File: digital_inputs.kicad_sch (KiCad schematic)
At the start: 12 parts, among them J3 Samtec Isorate, J5 Samtec Isorate, U6 SN74LV8T9541-EP, U7 SN74LV8T9541-EP

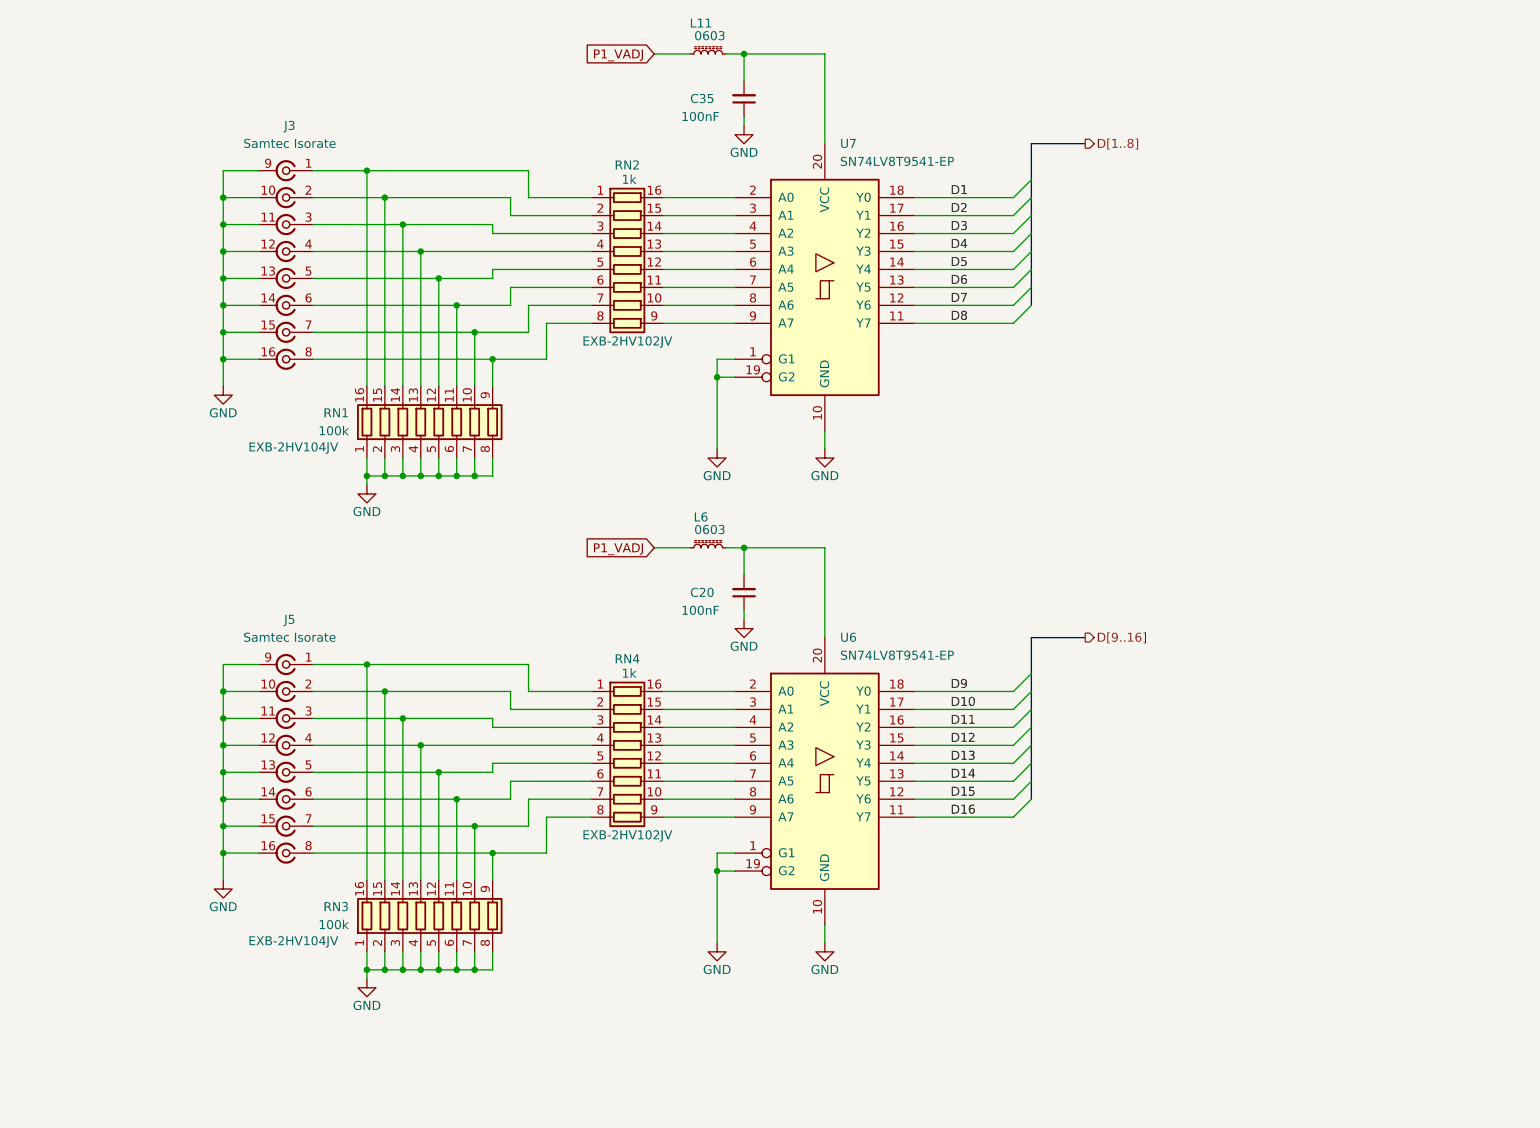
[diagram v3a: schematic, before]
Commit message: Draft Schematic Revision
Schematic should be in good shape.
Meta-data and BOM need to be finished.
Very rough layout was started to floorplan out main parts and to see if we have room.
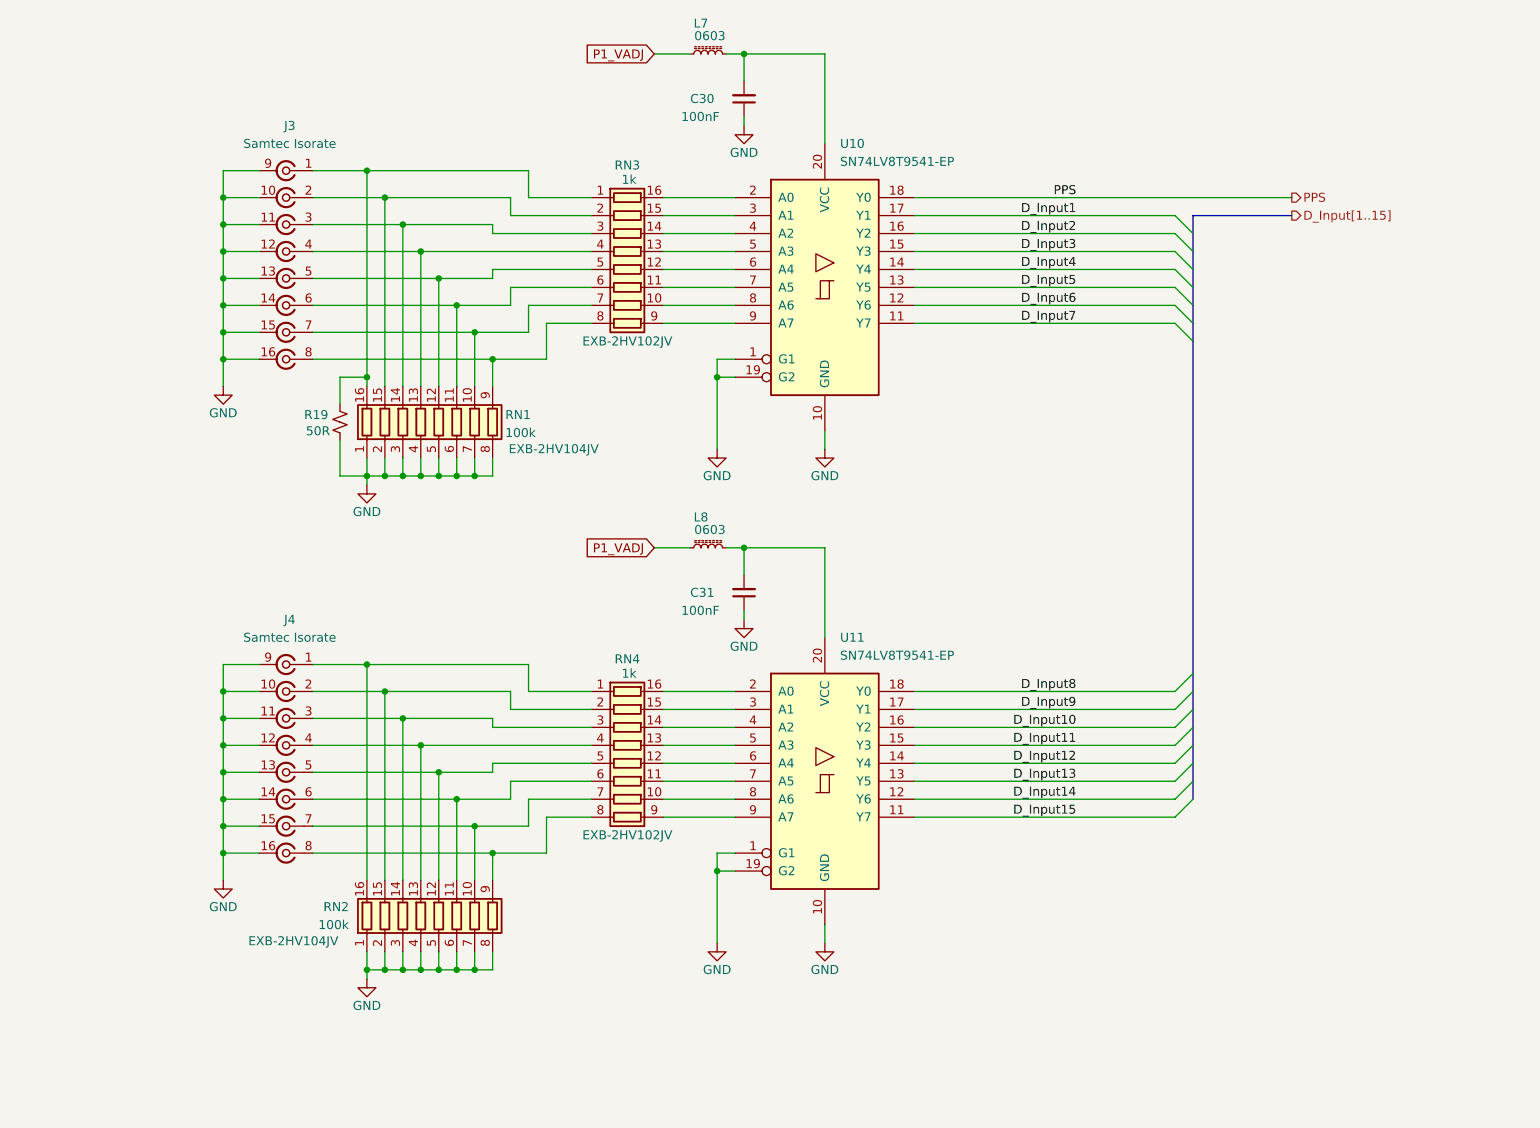
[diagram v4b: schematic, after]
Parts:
- added R19: 50R, Resistor_SMD:R_1206_3216Metric, symbol Device:R_Small_US
- J3: footprint (none) -> rf-input-fmc:SAMTEC_IP5-08-05.0-L-S-1-TR
- J4: renamed from J5; footprint (none) -> rf-input-fmc:SAMTEC_IP5-08-05.0-L-S-1-TR
- renumbered C35 to C30, C20 to C31, L11 to L7, L6 to L8, RN3 to RN2, RN2 to RN3, U7 to U10, U6 to U11
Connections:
- net GND: now also R19.2
- net at J3.1 (In), RN1.16 (R1.2), RN3.1 (R1.1): now also R19.1
- net D1 renamed PPS
- net D10 renamed D_Input9
- net D11 renamed D_Input10
- net D12 renamed D_Input11
- net D13 renamed D_Input12
- net D14 renamed D_Input13
- net D15 renamed D_Input14
- net D16 renamed D_Input15
- net D2 renamed D_Input1
- net D3 renamed D_Input2
- net D4 renamed D_Input3
- net D5 renamed D_Input4
- net D6 renamed D_Input5
- net D7 renamed D_Input6
- net D8 renamed D_Input7
- net D9 renamed D_Input8

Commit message: add copyright/license
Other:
- company: Osprey DCS -> SPDX-FileCopyrightText: 2025 Osprey DCS
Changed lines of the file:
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@@
 		(date "2025-10-01")
 		(rev "0.1")
-		(company "Osprey DCS")
-		(comment 1 "Pedro Rodriguez")
+		(company "SPDX-FileCopyrightText: 2025 Osprey DCS")
+		(comment 1 "SPDX-License-Identifier: CERN-OHL-S-2.0+")
 	)
 	(junction

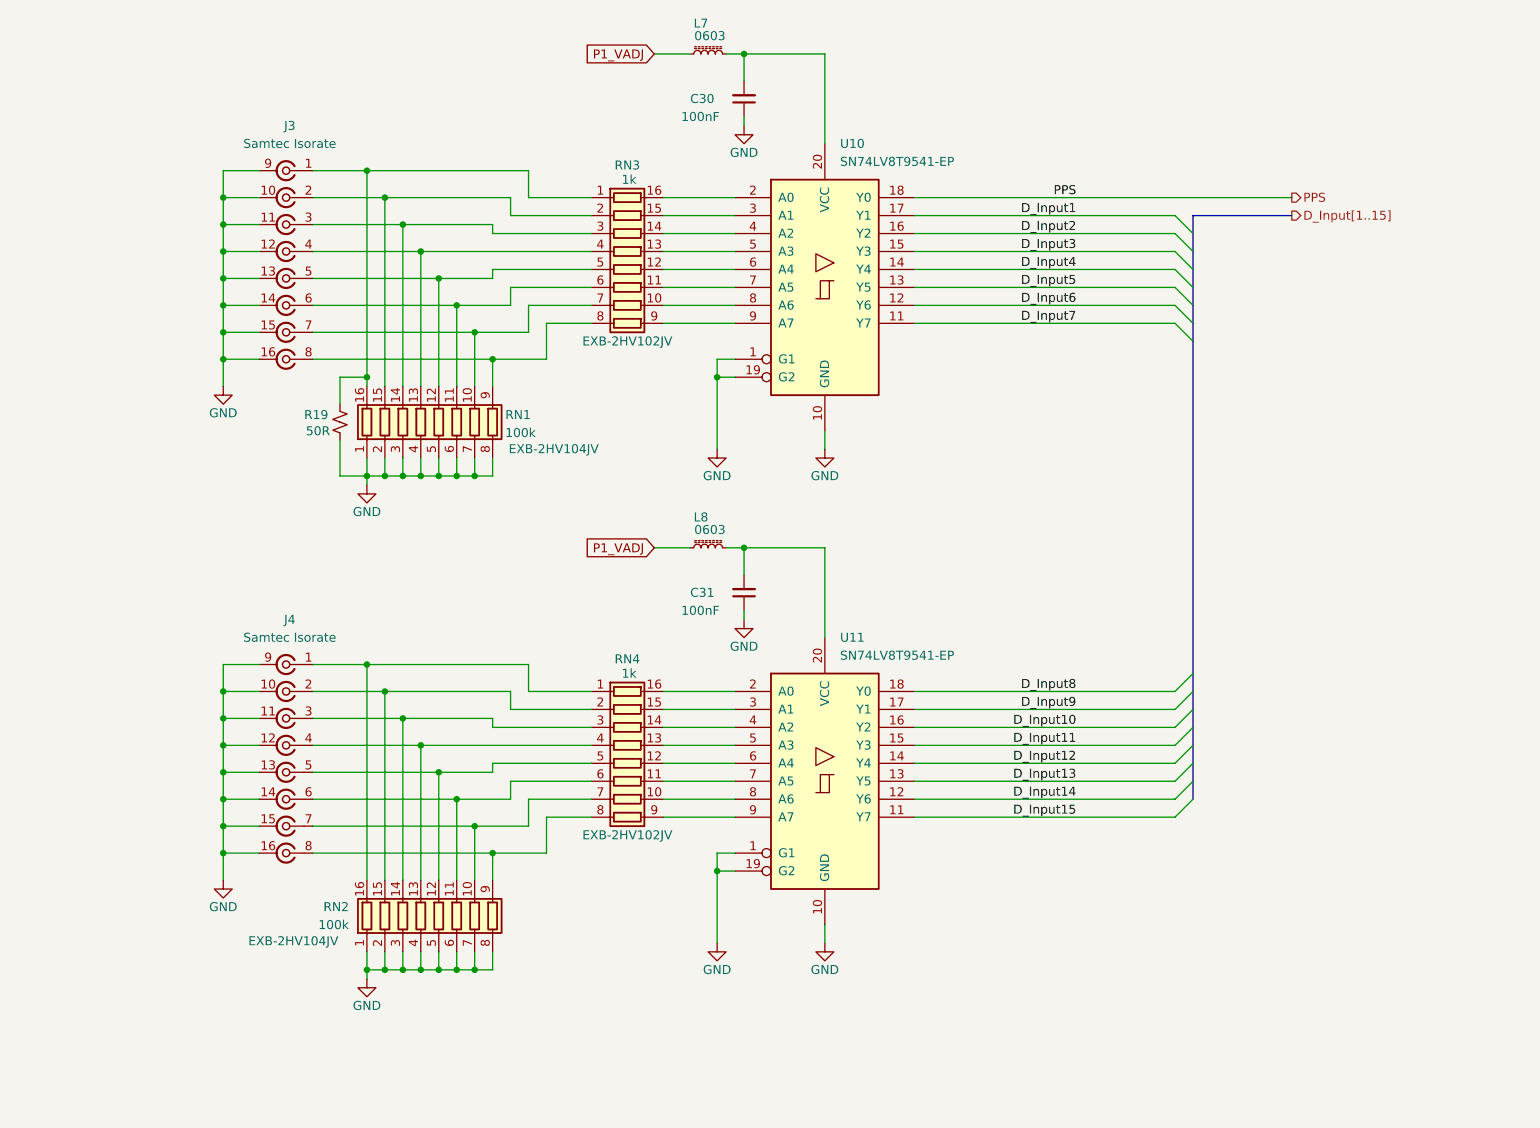
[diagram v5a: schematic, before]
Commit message: Changed ADC and removed Level Shifter
- Changed ADC to ADS7253
- Removed Level Shifters
- Change paper size to US standard sizes for printing
- removed 3d models
- Changed SMA clock input to a 2 pin ISORATE connector
- Floor planned out the PCB layout with the new parts
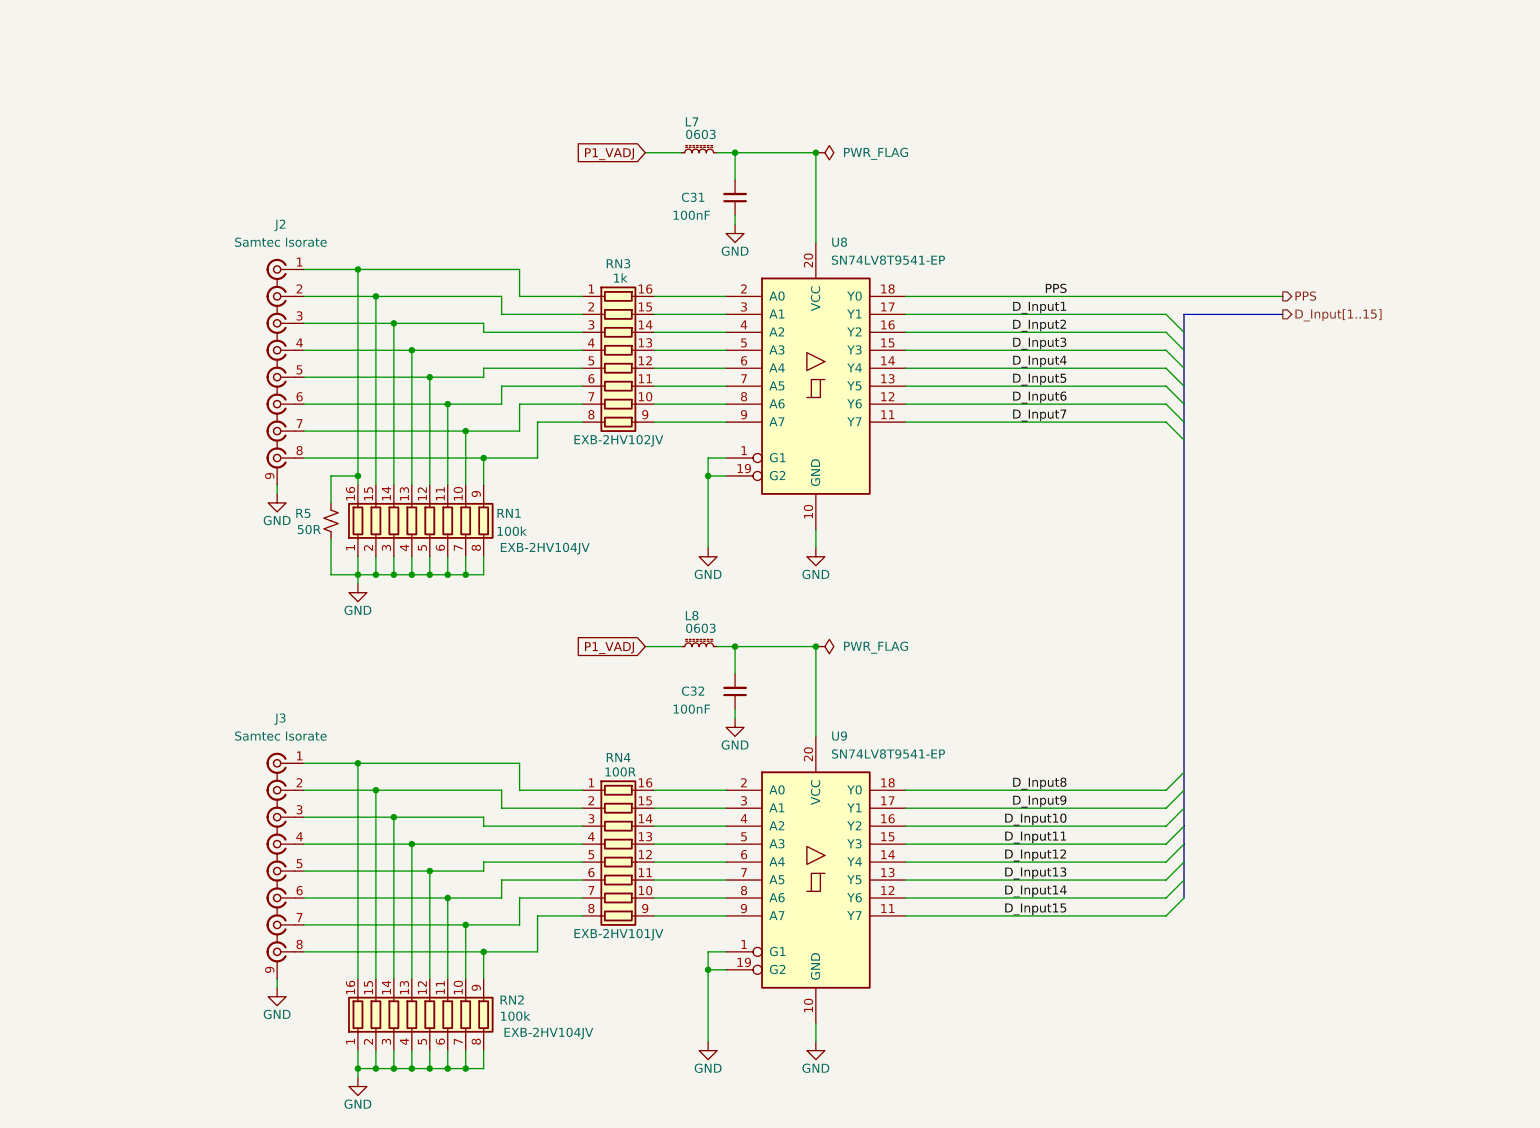
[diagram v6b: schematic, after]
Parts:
- J2: renamed from J3; footprint rf-input-fmc:SAMTEC_IP5-08-05.0-L-S-1-TR -> rf-input-fmc:SAMTEC_IP5-08-01-L-S-RA1-L-TR
- J3: renamed from J4; footprint rf-input-fmc:SAMTEC_IP5-08-05.0-L-S-1-TR -> rf-input-fmc:SAMTEC_IP5-08-01-L-S-RA1-L-TR
- RN4: value 1k -> 100R; MPN EXB-2HV102JV -> EXB-2HV101JV
- renumbered C30 to C31, C31 to C32, R19 to R5, U10 to U8, U11 to U9
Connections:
- net GND: no longer J2.10 (gnd), J2.11, J2.12 (gnd), J2.13 (gnd), J2.14 (gnd), J2.15 (gnd), J2.16 (gnd), J3.10 (gnd), J3.11, J3.12 (gnd), J3.13 (gnd), J3.14 (gnd), J3.15 (gnd), J3.16 (gnd)
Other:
- moved on the sheet: C31, C32, L7, L8, R5, RN1, RN2, RN3, RN4, U8, U9

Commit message: Final Schmatic Draft
-Changed ADC
-Changed Digital IO Translator
-Updated all MPNs
- Reannoted Schematic
- Updated Design Document
- Added new Datasheet Document
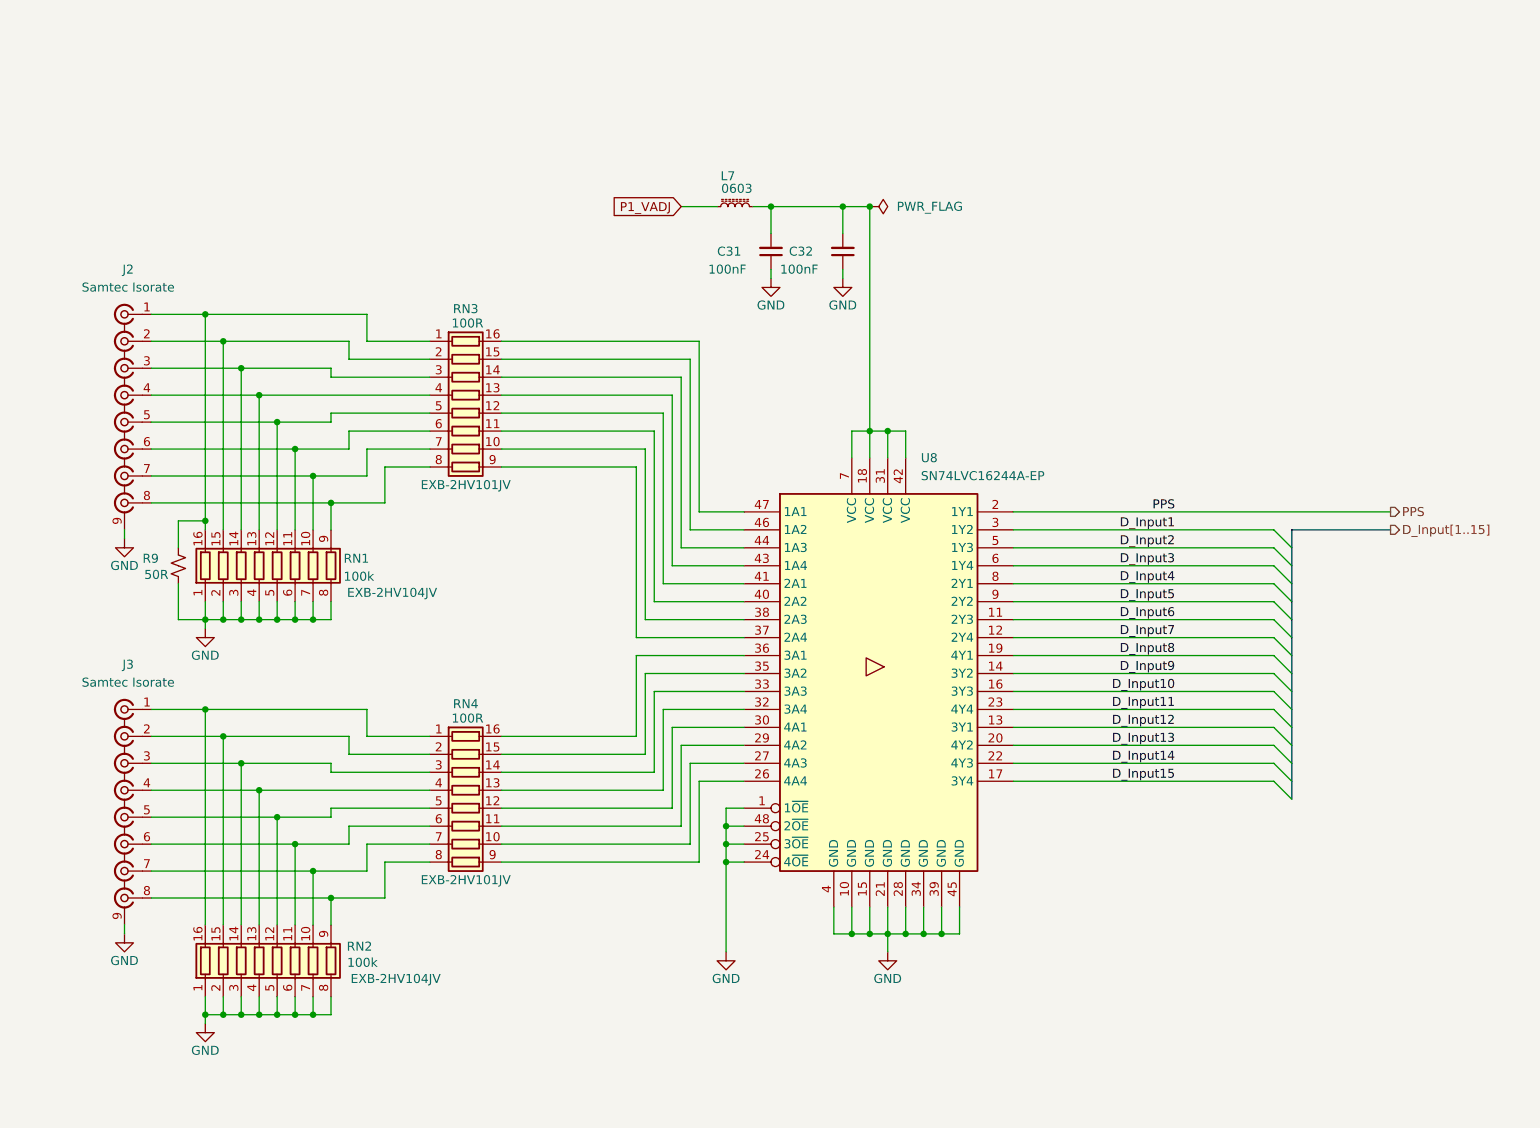
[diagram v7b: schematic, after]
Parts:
- removed L8: 0603, Inductor_SMD:L_0603_1608Metric, symbol Device:L_Ferrite_Small
- removed U8, U9: SN74LV8T9541-EP, Package_SO:TSSOP-20_4.4x6.5mm_P0.65mm, symbol 74xx:74AHC541
- added U8: SN74LVC16244A-EP, Package_SO:TSSOP-48_6.1x12.5mm_P0.5mm, symbol rf-input-fmc:SN74LVC16244A-EP
- J2, J3: MPN (none) -> SAMTEC_IP5-08-01-L-S-RA1-L-TR; Manufacturer (none) -> Samtec
- R9: renamed from R5; MPN (none) -> TNPW120650R0BEEN; Manufacturer (none) -> Vishay Dale
- RN1, RN2, RN4: Manufacturer (none) -> Panasonic Electronic Components
- RN3: value 1k -> 100R; MPN EXB-2HV102JV -> EXB-2HV101JV; Manufacturer (none) -> Panasonic Electronic Components
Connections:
- net D_Input1: now also U8.3 (1Y2)
- net D_Input10: now also U8.16 (3Y3)
- net D_Input11: now also U8.23 (4Y4)
- net D_Input12: now also U8.13 (3Y1)
- net D_Input13: now also U8.20 (4Y2)
- net D_Input14: now also U8.22 (4Y3)
- net D_Input15: now also U8.17 (3Y4)
- net D_Input2: now also U8.5 (1Y3)
- net D_Input3: now also U8.6 (1Y4)
- net D_Input4: now also U8.8 (2Y1)
- net D_Input5: now also U8.9 (2Y2)
- net D_Input6: now also U8.11 (2Y3)
- net D_Input7: now also U8.12 (2Y4)
- net D_Input8: now also U8.19 (4Y1)
- net D_Input9: now also U8.14 (3Y2)
- net GND: now also U8.1 (1~{OE}), U8.10 (GND), U8.15 (GND), U8.21 (GND), U8.24 (4~{OE}), U8.25 (3~{OE}), U8.28 (GND), U8.34 (GND), U8.39 (GND), U8.4 (GND), U8.45 (GND), U8.48 (2~{OE})
- net PPS: now also U8.2 (1Y1)
- net at RN3.16 (R1.2): now also U8.47 (1A1)
- net at C31.2, L7.2: now also C32.2, U8.18 (VCC), U8.31 (VCC), U8.42 (VCC), U8.7 (VCC)
- net at RN3.15 (R2.2): now also U8.46 (1A2)
- net at RN3.14 (R3.2): now also U8.44 (1A3)
- net at RN3.13 (R4.2): now also U8.43 (1A4)
- net at RN3.12 (R5.2): now also U8.41 (2A1)
- net at RN3.11 (R6.2): now also U8.40 (2A2)
- net at RN3.10 (R7.2): now also U8.38 (2A3)
- net at RN3.9 (R8.2): now also U8.37 (2A4)
- net at RN4.10 (R7.2): now also U8.27 (4A3)
- net at RN4.11 (R6.2): now also U8.29 (4A2)
- net at RN4.12 (R5.2): now also U8.30 (4A1)
- net at RN4.13 (R4.2): now also U8.32 (3A4)
- net at RN4.14 (R3.2): now also U8.33 (3A3)
- net at RN4.15 (R2.2): now also U8.35 (3A2)
- net at RN4.16 (R1.2): now also U8.36 (3A1)
- net at RN4.9 (R8.2): now also U8.26 (4A4)
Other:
- moved on the sheet: C31, J2, J3, L7, R9, RN1, RN2, RN3, RN4
